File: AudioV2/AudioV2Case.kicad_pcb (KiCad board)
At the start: 2 copper layers, 569.4 x 450 mm, 257 parts, among them J1601 AUDIO, J1602 V_IN, J1603 15_V_IN, J201 +15/A_GND/-15 out, J202 PD module in (1=GND 2=+12V), Q401 BSS138, Q402 BSS138, SW1601 DEST sense (3PDT 3rd pole, sa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, SW402 PWR SW, SW501 DEST L (PHONE/MUTE/LINE), SW502 DEST R (PHONE/MUTE/LINE), U1601 OPA1656, U1602 OPA1656, U1603 LT1763-3.3, U1605 TPS3307-33, U1606 LT1763-5, U1607 BP5293-50, U1608 OPA1656, U1609 XC8107AC20MR-G, U1610 MCP23017 (UI 0x22), U1611 OPA1656, U201 REC20K-2415DZ, U202 L7809CV +9V, U311 TMUX7612, U312 TMUX7612, U402 PT2314E, U403 BP5293-50 +5V, U501 OPA1652, Y1601 ASFL1-12.288MHZ-EC-T

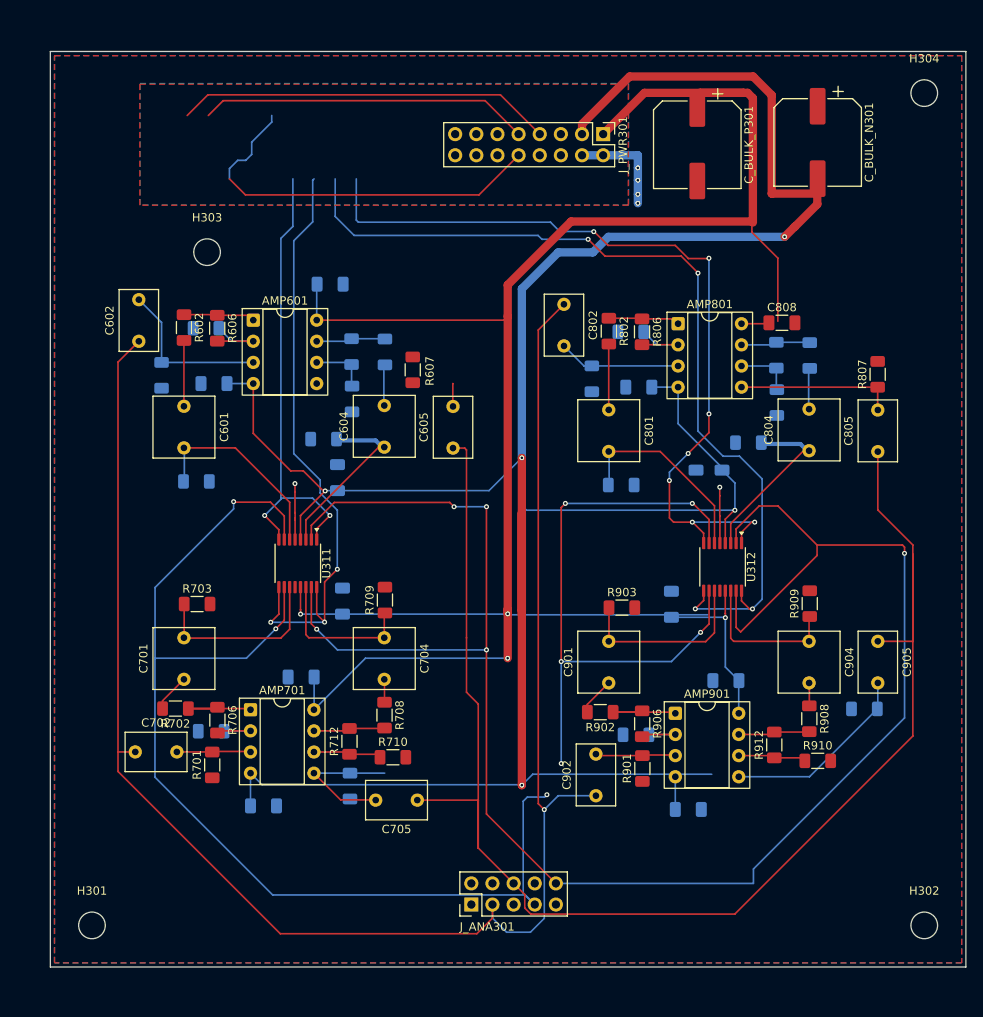
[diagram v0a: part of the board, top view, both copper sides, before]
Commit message: AudioV2: 娘を縮小し AMP_SEL を裏へ、A_GND ステッチと Rf/Rg を 0805 に
表の AMP_SEL 幹線を裏本線にし、TMUX デカップと電源幅をピン周りで寄せた。A_GND ビアを TMUX / SEL 脇に足す。比較用 20k は 0805。

Co-authored-by: Cursor <cursoragent@cursor.com>
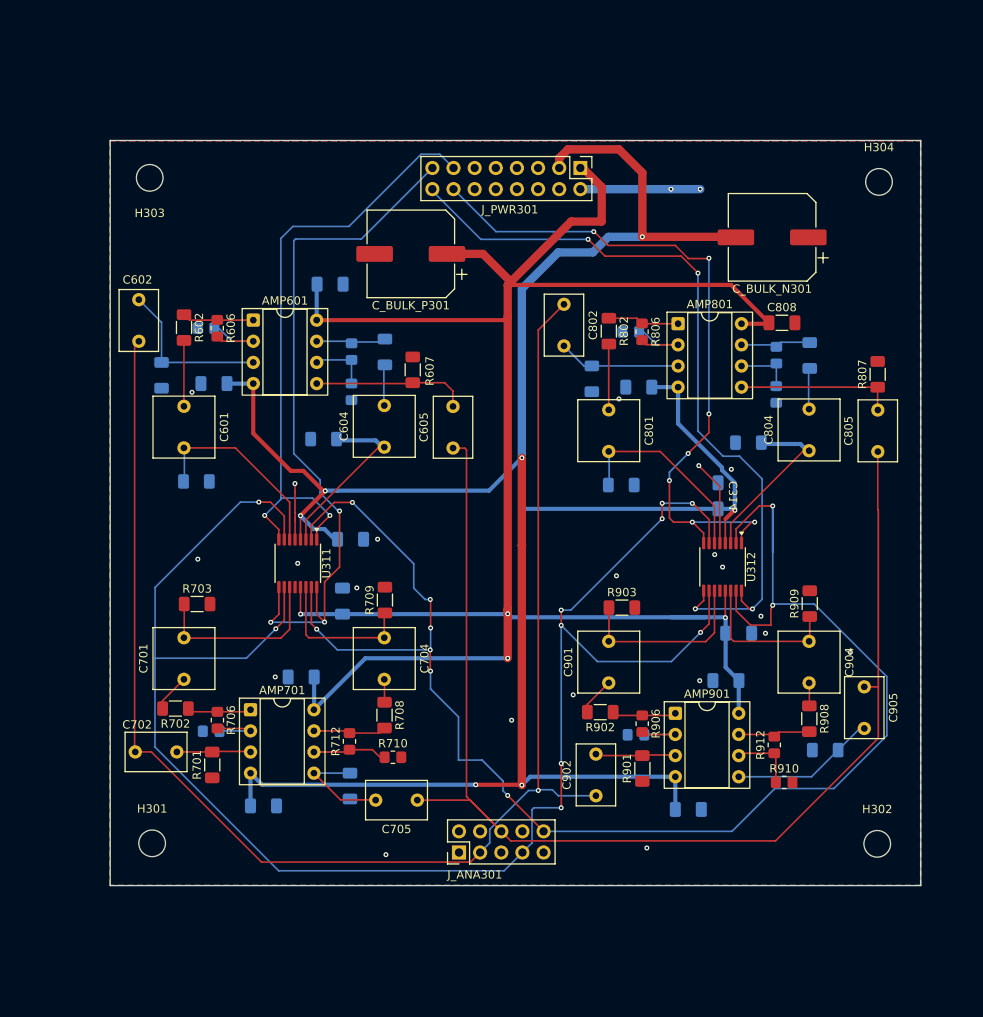
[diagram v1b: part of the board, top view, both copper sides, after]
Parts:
- R604, R606, R610, R612, R704, R706, R710, R712, R804, R806, R810, R812, R904, R906, R910, R912: footprint Resistor_SMD:R_1206_3216Metric_Pad1.30x1.75mm_HandSolder -> Resistor_SMD:R_0805_2012Metric_Pad1.20x1.40mm_HandSolder
- moved C_BULK_P301 36.8 mm to (507.7, 136.3), turned to 180 degrees
- moved C_BULK_N301 12.6 mm to (551.1, 134.3), turned to 180 degrees
- moved H301 12.2 mm to (476.6, 207.1)
- moved H304 12.0 mm to (563.9, 127.7)
- moved H302 11.3 mm to (563.7, 207.2)
- moved H303 11.3 mm to (476.3, 127.2)
- moved C313 8.80 mm to (547.1, 181.9), turned to 0 degrees
- moved C312 7.57 mm to (500.4, 170.6), turned to 180 degrees
- moved R907 6.83 mm to (557.5, 195.9)
- moved J_ANA301 6.43 mm to (513.5, 208.2)
- moved C905 5.71 mm to (562.2, 188.3)
- moved J_PWR301 4.91 mm to (528.1, 126.0)
- moved R910 4.79 mm to (552.5, 199.8)
- moved C314 3.27 mm to (544.6, 165.4), turned to -90 degrees
- moved R810 0.97 mm to (551.6, 153.2)
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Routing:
- net /-15V: track 343.6 -> 283.8 mm, vias 5 -> 7
- net unconnected-(J_PWR301-Pin_7-Pad7): track 45.3 -> 0.00 mm
- net unconnected-(J_PWR301-Pin_9-Pad9): track 39.7 -> 0.00 mm
- net unconnected-(J_PWR301-Pin_10-Pad10): track 37.5 -> 0.00 mm
- net /AMP_SEL_R: track 215.7 -> 183.9 mm, vias 5 -> 9
- net /TONE_R: track 179.1 -> 149.2 mm
- net /TONE_L: track 201.8 -> 174.9 mm
- net /+15V: track 268.4 -> 244.4 mm
- net /SLOT1_SEL_CH1: track 55.8 -> 73.6 mm
- net Net-(AMP601B-+): track 2.76 -> 18.7 mm
- net /SLOT1_SEL_CH3: track 99.4 -> 84.3 mm
- net /SLOT1_SEL_CH4: track 108.5 -> 93.8 mm
- net /SLOT1_SEL_CH2: track 72.7 -> 84.9 mm
- net /AMP_SEL_L: track 212.1 -> 201.3 mm, vias 8 -> 10
- net /3V3: track 10.3 -> 0.00 mm
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- removed copper zone on B.Cu, net /D_GND
- removed copper zone on F.Cu, net /D_GND
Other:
- board size 569.4 x 450 mm -> 564 x 450 mm

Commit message: AudioV2: FrontPanel を母板直下へ、渡りを XH 列分割に
操作系を FrontPanel 子シートに切り出し母板直下へ載せ替え、母板↔パネル渡りを
奇偶列の XH（*_1/*_2）にした。PCB から分割前の PinHeader 孤児を除去し、
Cosland トグル FP と関連スクリプトも同梱する。

Co-authored-by: Cursor <cursoragent@cursor.com>
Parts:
- removed LCDDisplay1601: WAVESHARE-29318, Connector_PinHeader_2.54mm:PinHeader_1x15_P2.54mm_Vertical
- removed SW1601: DEST sense (3PDT 3rd pole, same body as SW501/SW502), Connector_PinHeader_2.54mm:PinHeader_1x04_P2.54mm_Vertical
- removed SW502: DEST R (PHONE/MUTE/LINE), Connector_PinHeader_2.54mm:PinHeader_1x04_P2.54mm_Vertical
- added J_PNL1601_1: FrontPanel digital A (odd), Connector_JST:JST_XH_B10B-XH-A_1x10_P2.50mm_Vertical, F.Cu at (205.7, 427.1)
- added J_PNL1601_2: FrontPanel digital B (even), Connector_JST:JST_XH_B10B-XH-A_1x10_P2.50mm_Vertical, F.Cu at (205.7, 434.9)
- added J_PNL1602_1: FrontPanel digital A (odd), Connector_JST:JST_XH_B10B-XH-A_1x10_P2.50mm_Vertical, F.Cu at (22.8, 542.0)
- added J_PNL1602_2: FrontPanel digital B (even), Connector_JST:JST_XH_B10B-XH-A_1x10_P2.50mm_Vertical, F.Cu at (22.8, 549.8)
- added J_PNL_A1601_1: FrontPanel analog A (odd), Connector_JST:JST_XH_B8B-XH-A_1x08_P2.50mm_Vertical, F.Cu at (222.7, 446.8)
- added J_PNL_A1601_2: FrontPanel analog B (even), Connector_JST:JST_XH_B8B-XH-A_1x08_P2.50mm_Vertical, F.Cu at (193.2, 446.7)
- added J_PNL_A1602_1: FrontPanel analog A (odd), Connector_JST:JST_XH_B8B-XH-A_1x08_P2.50mm_Vertical, F.Cu at (22.8, 557.6)
- added J_PNL_A1602_2: FrontPanel analog B (even), Connector_JST:JST_XH_B8B-XH-A_1x08_P2.50mm_Vertical, F.Cu at (22.8, 565.4)
- added LCDDisplay1601_1: FrontPanel analog B (even), Connector_JST:JST_XH_B8B-XH-A_1x08_P2.50mm_Vertical, F.Cu at (25.4, 520.5)
- added LCDDisplay1601_2: FrontPanel analog B (even), Connector_JST:JST_XH_B8B-XH-A_1x08_P2.50mm_Vertical, F.Cu at (25.4, 528.3)
- J_HP501, J_LINE501: footprint TerminalBlock_Phoenix:TerminalBlock_Phoenix_MKDS-1,5-3-5.08_1x03_P5.08mm_Horizontal -> Connector_JST:JST_XH_B3B-XH-A_1x03_P2.50mm_Vertical
- J_OLED1601: footprint Connector_PinHeader_2.54mm:PinHeader_1x04_P2.54mm_Vertical -> Connector_JST:JST_XH_B4B-XH-A_1x04_P2.50mm_Vertical
- R401: value 2.2k -> 1k
- RV501, RV502: footprint Connector_PinHeader_2.54mm:PinHeader_1x06_P2.54mm_Vertical -> Connector_JST:JST_XH_B6B-XH-A_1x06_P2.50mm_Vertical
- SW402: value PWR SW -> Cosland 2MS1 PWR; footprint Connector_PinHeader_2.54mm:PinHeader_1x02_P2.54mm_Vertical -> Library:SW_Toggle_Cosland_2MS1_VS2_SPDT
- SW501: value DEST L (PHONE/MUTE/LINE) -> Cosland 2MD1 DEST; footprint Connector_PinHeader_2.54mm:PinHeader_1x04_P2.54mm_Vertical -> Library:SW_Toggle_Cosland_2MD1_VS2_DPDT
- moved D403 475.1 mm to (42.0, 500.0)
- moved R401 473.8 mm to (42.0, 512.0), turned to 90 degrees
- moved C1629 258.1 mm to (105.0, 580.0)
- moved C1630 243.1 mm to (105.0, 568.0)
- moved C1631 242.6 mm to (115.0, 568.0)
- moved C1633 239.3 mm to (125.0, 568.0)
- moved C1650 231.4 mm to (108.0, 575.0)
- moved J_HP501 225.2 mm to (114.2, 474.7)
- moved J_LINE501 225.1 mm to (99.4, 474.7)
- moved R1662 215.0 mm to (75.0, 585.0)
- moved U1610 207.1 mm to (90.0, 575.0)
- moved R1661 205.4 mm to (75.0, 575.0)
- moved R1620 200.0 mm to (115.0, 555.0), turned to 90 degrees
- moved U1609 190.6 mm to (125.0, 555.0)
- moved R1651 133.4 mm to (140.0, 518.0), turned to 90 degrees
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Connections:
- net /LED_12V_A renamed /FrontPanel/LED_12V_A
- net /MeasureControl/+5V_D renamed /+5V_D
- net /MeasureControl/ENC1_A renamed /FrontPanel/ENC1_A
- net /MeasureControl/ENC1_B renamed /FrontPanel/ENC1_B
- net /MeasureControl/ENC1_SW renamed /FrontPanel/ENC1_SW
- net /MeasureControl/ENC2_A renamed /FrontPanel/ENC2_A
- net /MeasureControl/ENC2_B renamed /FrontPanel/ENC2_B
- net /MeasureControl/ENC2_SW renamed /FrontPanel/ENC2_SW
- net /MeasureControl/ENC3_A renamed /FrontPanel/ENC3_A
- net /MeasureControl/ENC3_B renamed /FrontPanel/ENC3_B
- net /MeasureControl/ENC3_SW renamed /FrontPanel/ENC3_SW
- net /MeasureControl/ENC_INTA renamed /ENC_INTA
- net /MeasureControl/ENC_INTB renamed /ENC_INTB
- net /MeasureControl/LCD_EN renamed /LCD_EN
- net /MeasureControl/LCD_VCC renamed /FrontPanel/LCD_VCC
- net /MeasureControl/LED_DEST1 renamed /FrontPanel/LED_DEST1
- net /MeasureControl/LED_DEST1_A renamed /FrontPanel/LED_DEST1_A
- net /MeasureControl/LED_DEST2 renamed /FrontPanel/LED_DEST2
- net /MeasureControl/LED_DEST2_A renamed /FrontPanel/LED_DEST2_A
- net /PHONE_PRE_L renamed /FrontPanel/PHONE_PRE_L
- A1602 pad 10: /MeasureControl/LCD_RST -> /LCD_RST
- A1602 pad 14: /MeasureControl/TP_SDA -> /TP_SDA
- A1602 pad 15: /MeasureControl/TP_SCL -> /TP_SCL
- A1602 pad 16: /MeasureControl/TP_INT -> /TP_INT
- A1602 pad 17: /MeasureControl/TP_RST -> /TP_RST
- A1602 pad 24: /MeasureControl/LCD_SCK -> /LCD_SCK
- A1602 pad 25: /MeasureControl/LCD_MOSI -> /LCD_MOSI
- A1602 pad 7: /MeasureControl/LCD_CS -> /LCD_CS
- A1602 pad 9: /MeasureControl/LCD_DC -> /LCD_DC
- R1655 pad 2: /MeasureControl/DEST_SENSE_LINE -> /MeasureControl/FrontPanel/DEST_SENSE_LINE
- R1658 pad 1: /MeasureControl/DEST_SENSE_PHONE -> /MeasureControl/FrontPanel/DEST_SENSE_PHONE
- RV501 pad 4: /PHONE_PRE_R -> /FrontPanel/PHONE_PRE_R
- RV502 pad 1: /LINE_PRE_L -> /FrontPanel/LINE_PRE_L
- RV502 pad 4: /LINE_PRE_R -> /FrontPanel/LINE_PRE_R
- SW402 pad 1: /PD_12V -> /PD_12V_SW
- SW402 pad 2: /PD_12V_SW -> /PD_12V
- SW501 pad 2: unconnected-(SW501-Pad2) -> /AMP_SEL_L
- SW501 pad 3: /AMP_SEL_L -> /FrontPanel/LINE_PRE_L
- SW501 pad 4: /LINE_PRE_L -> /FrontPanel/PHONE_PRE_R
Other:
- board size 564 x 450 mm -> 564 x 575 mm

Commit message: AudioV2: FrontPanel の 12V を電源 XH に分離し FP PCB を配線
音声 XH から PD を外し J_PNL_P* へ移す。A/D/PD の GND 同居を避け、
FrontPanel 側のデジ・音声・電源配線とベタ分けを進めた。

Co-authored-by: Cursor <cursoragent@cursor.com>
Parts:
- removed R1655, R1658: 1k, Resistor_SMD:R_1206_3216Metric_Pad1.30x1.75mm_HandSolder
- removed R1656: 10k, Resistor_SMD:R_1206_3216Metric_Pad1.30x1.75mm_HandSolder
- added J_PNL_P1601: FrontPanel 12V raw, Connector_JST:JST_XH_B3B-XH-A_1x03_P2.50mm_Vertical, F.Cu at (365.3, 448.1)
- added J_PNL_P1602: FrontPanel 12V switched, Connector_JST:JST_XH_B3B-XH-A_1x03_P2.50mm_Vertical, F.Cu at (384.4, 448.6)
- added J_PNL_P1611: FrontPanel 12V raw, Connector_JST:JST_XH_B3B-XH-A_1x03_P2.50mm_Vertical, B.Cu at (177.8, 491.8)
- added J_PNL_P1612: FrontPanel 12V switched, Connector_JST:JST_XH_B3B-XH-A_1x03_P2.50mm_Vertical, B.Cu at (175.6, 520.2)
- C1629, C1630, C1631, C1633, C1650, J_OLED1601, J_PNL1602_1, J_PNL1602_2, J_PNL_A1602_1, R1620, RV501, RV502, U1609, U1610: moved to B.Cu
- J_LCD1601: renamed from LCDDisplay1601_1; value FrontPanel analog B (even) -> LCD cable A (XH8); moved to B.Cu
- J_LCD1602: renamed from LCDDisplay1601_2; value FrontPanel analog B (even) -> LCD cable B (XH8); moved to B.Cu
- J_PNL_A1602_2: value FrontPanel analog B (even) -> LCD cable A (XH8); moved to B.Cu
- moved J_PNL_A1602_2 318.5 mm to (334.0, 497.8), turned to 90 degrees
- moved J_LINE501 282.5 mm to (377.6, 425.8)
- moved J_PNL_A1602_1 280.3 mm to (300.4, 518.4), turned to 90 degrees
- moved J_HP501 265.7 mm to (377.6, 440.2)
- moved J_PNL1602_1 250.8 mm to (265.5, 478.8)
- moved J_OLED1601 214.2 mm to (274.6, 519.2), turned to 180 degrees
- moved J_LCD1601 206.4 mm to (231.5, 530.2)
- moved R1652 201.1 mm to (340.6, 513.9), turned to 0 degrees
- moved R1661 199.2 mm to (250.1, 479.9), turned to 180 degrees
- moved R1662 199.2 mm to (244.3, 480.1)
- moved U1610 197.0 mm to (268.5, 491.7), turned to 90 degrees
- moved D1611 192.8 mm to (339.7, 506.8)
- moved R1651 188.3 mm to (328.3, 513.9), turned to 0 degrees
- moved RV501 187.1 mm to (306.7, 492.4)
- moved D1610 179.7 mm to (327.3, 506.8)
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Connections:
- J_PNL_A1601_1 pad 5: /PD_12V -> unconnected-(J_PNL_A1601_1-Pin_5-Pad5)
- J_PNL_A1601_1 pad 6: /PD_GND -> unconnected-(J_PNL_A1601_1-Pin_6-Pad6)
- J_PNL_A1601_2 pad 5: /PD_12V_SW -> unconnected-(J_PNL_A1601_2-Pin_5-Pad5)
- J_PNL_A1602_1 pad 5: /PD_12V -> unconnected-(J_PNL_A1602_1-Pin_5-Pad5)
- J_PNL_A1602_1 pad 6: /PD_GND -> unconnected-(J_PNL_A1602_1-Pin_6-Pad6)
- J_PNL_A1602_2 pad 5: /PD_12V_SW -> unconnected-(J_PNL_A1602_2-Pin_5-Pad5)
- U1610 pad 2: /FrontPanel/LED_DEST1 -> /FrontPanel/LED_DEST2
- U1610 pad 3: /FrontPanel/LED_DEST2 -> /FrontPanel/LED_DEST1
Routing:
- net /3V3: track 0.00 -> 185.5 mm
- net /FrontPanel/LED_DEST1: track 0.00 -> 132.1 mm
- net /FrontPanel/LED_DEST2: track 0.00 -> 118.4 mm
- net /I2C_SCL: track 0.00 -> 103.8 mm
- net /I2C_SDA: track 0.00 -> 100.8 mm
- net /TP_INT: track 0.00 -> 98.5 mm
- net /TP_SDA: track 0.00 -> 97.5 mm
- net /LCD_RST: track 0.00 -> 94.0 mm
- net /LCD_SCK: track 0.00 -> 85.4 mm, vias 0 -> 2
- net /LCD_CS: track 0.00 -> 80.2 mm, vias 0 -> 1
- net /FrontPanel/LCD_VCC: track 0.00 -> 75.8 mm
- net /ENC_INTB: track 0.00 -> 68.8 mm, vias 0 -> 1
- net /D_GND: track 0.00 -> 53.4 mm, vias 0 -> 10
- net /TP_SCL: track 0.00 -> 53.2 mm, vias 0 -> 1
- net /FrontPanel/ENC1_B: track 0.00 -> 53.2 mm
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- added copper zone on B.Cu, net /D_GND
- added copper zone on F.Cu, net /D_GND
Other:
- board size 564 x 575 mm -> 564 x 531.4 mm
- board text added: "FRONT PANEL"
